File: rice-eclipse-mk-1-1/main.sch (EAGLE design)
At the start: 4 parts

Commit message: Added some new voltage regulators and used them. I also did something else, but I'm not sure what it was.
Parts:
- added ADC_X: AD7124-8BCPZ, analog-devices-extra-AD7124-8BCPZ:AD7124-8BCPZ
- added C3: 1UF, resistor:C-USC0603
- added C4, C6, C7: 10UF, rcl:C-US025-050X050
- added C5: 100UF, rcl:C-US025-050X050
- added REG1: AP2210N-3.3TRG1, diodes-extra:AP2210N-3.3TRG1
- added U1: LM1084ISX-5.0/NOPB, texas-extra:LM1084ISX-5.0/NOPB
- ADC1: value AD7124-8BCPZ -> MCP3208SN; device analog-devices-extra-AD7124-8BCPZ:AD7124-8BCPZ -> microchip-extra:MCP3208SN
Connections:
- new net +5V: C7.1, U1.VOUT
- new net AGND: ADC1.AGND, C3.2
- net +12V: now also C5.1, C6.1, REG1.VIN, U1.VIN
- net +3.3V: now also ADC1.VDD, ADC1.VREF, ADC_X.AVDD, ADC_X.IOVDD, C3.1, C4.1, REG1.VOUT; no longer ADC1.AVDD, ADC1.IOVDD
- net ADC1_A0: now also ADC1.CH0, ADC_X.AIN0/IOUT/VBIAS; no longer ADC1.AIN0/IOUT/VBIAS
- net ADC1_A1: now also ADC1.CH1, ADC_X.AIN1/IOUT/VBIAS; no longer ADC1.AIN1/IOUT/VBIAS
- net ADC1_A10: now also ADC_X.AIN10/IOUT/VBIAS; no longer ADC1.AIN10/IOUT/VBIAS
- net ADC1_A11: now also ADC_X.AIN11/IOUT/VBIAS; no longer ADC1.AIN11/IOUT/VBIAS
- net ADC1_A12: now also ADC_X.AIN12/IOUT/VBIAS; no longer ADC1.AIN12/IOUT/VBIAS
- net ADC1_A14: now also ADC_X.AIN14/IOUT/VBIAS/REFIN2(+); no longer ADC1.AIN14/IOUT/VBIAS/REFIN2(+)
- net ADC1_A15: now also ADC_X.AIN15/IOUT/VBIAS/REFIN2(-); no longer ADC1.AIN15/IOUT/VBIAS/REFIN2(-)
- net ADC1_A2: now also ADC1.CH2, ADC_X.AIN2/IOUT/VBIAS/P1; no longer ADC1.AIN2/IOUT/VBIAS/P1
- net ADC1_A3: now also ADC1.CH3, ADC_X.AIN3/IOUT/VBIAS/P2; no longer ADC1.AIN3/IOUT/VBIAS/P2
- net ADC1_A4: now also ADC1.CH4, ADC_X.AIN4/IOUT/VBIAS/P3; no longer ADC1.AIN4/IOUT/VBIAS/P3
- net ADC1_A5: now also ADC1.CH5, ADC_X.AIN5/IOUT/VBIAS/P4; no longer ADC1.AIN5/IOUT/VBIAS/P4
- net ADC1_A6: now also ADC1.CH6, ADC_X.AIN6/IOUT/VBIAS; no longer ADC1.AIN6/IOUT/VBIAS
- net ADC1_A7: now also ADC1.CH7, ADC_X.AIN7/IOUT/VBIAS; no longer ADC1.AIN7/IOUT/VBIAS
- net ADC1_A8: now also ADC_X.AIN8/IOUT/VBIAS; no longer ADC1.AIN8/IOUT/VBIAS
- net ADC1_A9: now also ADC_X.AIN9/IOUT/VBIAS; no longer ADC1.AIN9/IOUT/VBIAS
- net CS: now also ADC_X.*CS; no longer ADC1.*CS
- net DGND: now also ADC_X.AVSS, ADC_X.DGND, ADC_X.EP; no longer ADC1.AVSS, ADC1.EP
- net GND: now also C4.2, C5.2, C6.2, C7.2, REG1.GND, U1.GND
- net MISO: now also ADC_X.DOUT/*RDY; no longer ADC1.DOUT/*RDY
- net MOSI: now also ADC_X.DIN; no longer ADC1.DIN
- net N$1: now also ADC_X.REGCAPD; no longer ADC1.REGCAPD
- net N$2: now also ADC_X.REGCAPA; no longer ADC1.REGCAPA
- net SCLK: now also ADC_X.SCLK; no longer ADC1.SCLK

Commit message: Added a shorts library and some skeleton sheets in the schematic. Should provide a good environment for working on project.
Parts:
- removed ADC_X: AD7124-8BCPZ, analog-devices-extra-AD7124-8BCPZ:AD7124-8BCPZ
- removed C1, C2: 0.1UF, resistor:C-USC0603
- added SH1: SHORTT5, shorts:SHORTT5
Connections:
- removed net +3.3V: ADC1.VDD, ADC1.VREF, ADC_X.AVDD, ADC_X.IOVDD, C3.1, C4.1, REG1.VOUT
- removed net ADC1_A10: ADC_X.AIN10/IOUT/VBIAS
- removed net ADC1_A11: ADC_X.AIN11/IOUT/VBIAS
- removed net ADC1_A12: ADC_X.AIN12/IOUT/VBIAS
- removed net ADC1_A14: ADC_X.AIN14/IOUT/VBIAS/REFIN2(+)
- removed net ADC1_A15: ADC_X.AIN15/IOUT/VBIAS/REFIN2(-)
- removed net ADC1_A8: ADC_X.AIN8/IOUT/VBIAS
- removed net ADC1_A9: ADC_X.AIN9/IOUT/VBIAS
- removed net CS: ADC_X.*CS
- removed net MISO: ADC_X.DOUT/*RDY
- removed net MOSI: ADC_X.DIN
- removed net N$1: ADC_X.REGCAPD, C2.1
- removed net N$2: ADC_X.REGCAPA, C1.1
- removed net SCLK: ADC_X.SCLK
- new net +3V3: ADC1.VDD, ADC1.VREF, C3.1, C4.1, REG1.VOUT
- new net TEST_NET_1: SH1.P$1
- new net TEST_NET_2: SH1.P$2
- net ADC1_A0: no longer ADC_X.AIN0/IOUT/VBIAS
- net ADC1_A1: no longer ADC_X.AIN1/IOUT/VBIAS
- net ADC1_A2: no longer ADC_X.AIN2/IOUT/VBIAS/P1
- net ADC1_A3: no longer ADC_X.AIN3/IOUT/VBIAS/P2
- net ADC1_A4: no longer ADC_X.AIN4/IOUT/VBIAS/P3
- net ADC1_A5: no longer ADC_X.AIN5/IOUT/VBIAS/P4
- net ADC1_A6: no longer ADC_X.AIN6/IOUT/VBIAS
- net ADC1_A7: no longer ADC_X.AIN7/IOUT/VBIAS
- net DGND: no longer ADC_X.AVSS, ADC_X.DGND, ADC_X.EP, C1.2, C2.2

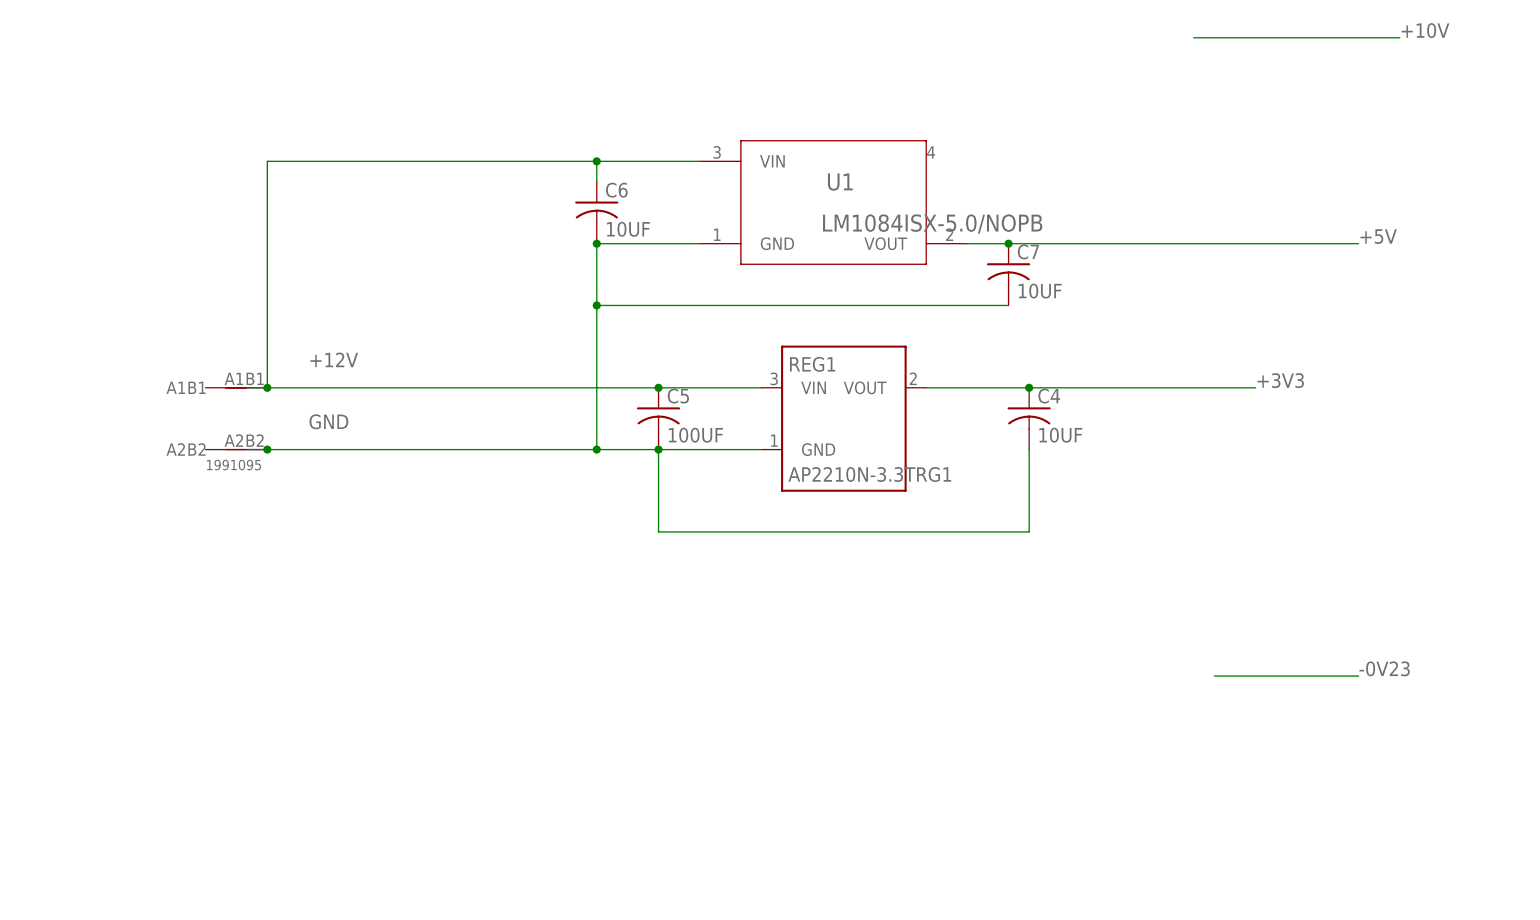
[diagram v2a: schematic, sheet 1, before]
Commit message: Added voltage regulator for -0.23v
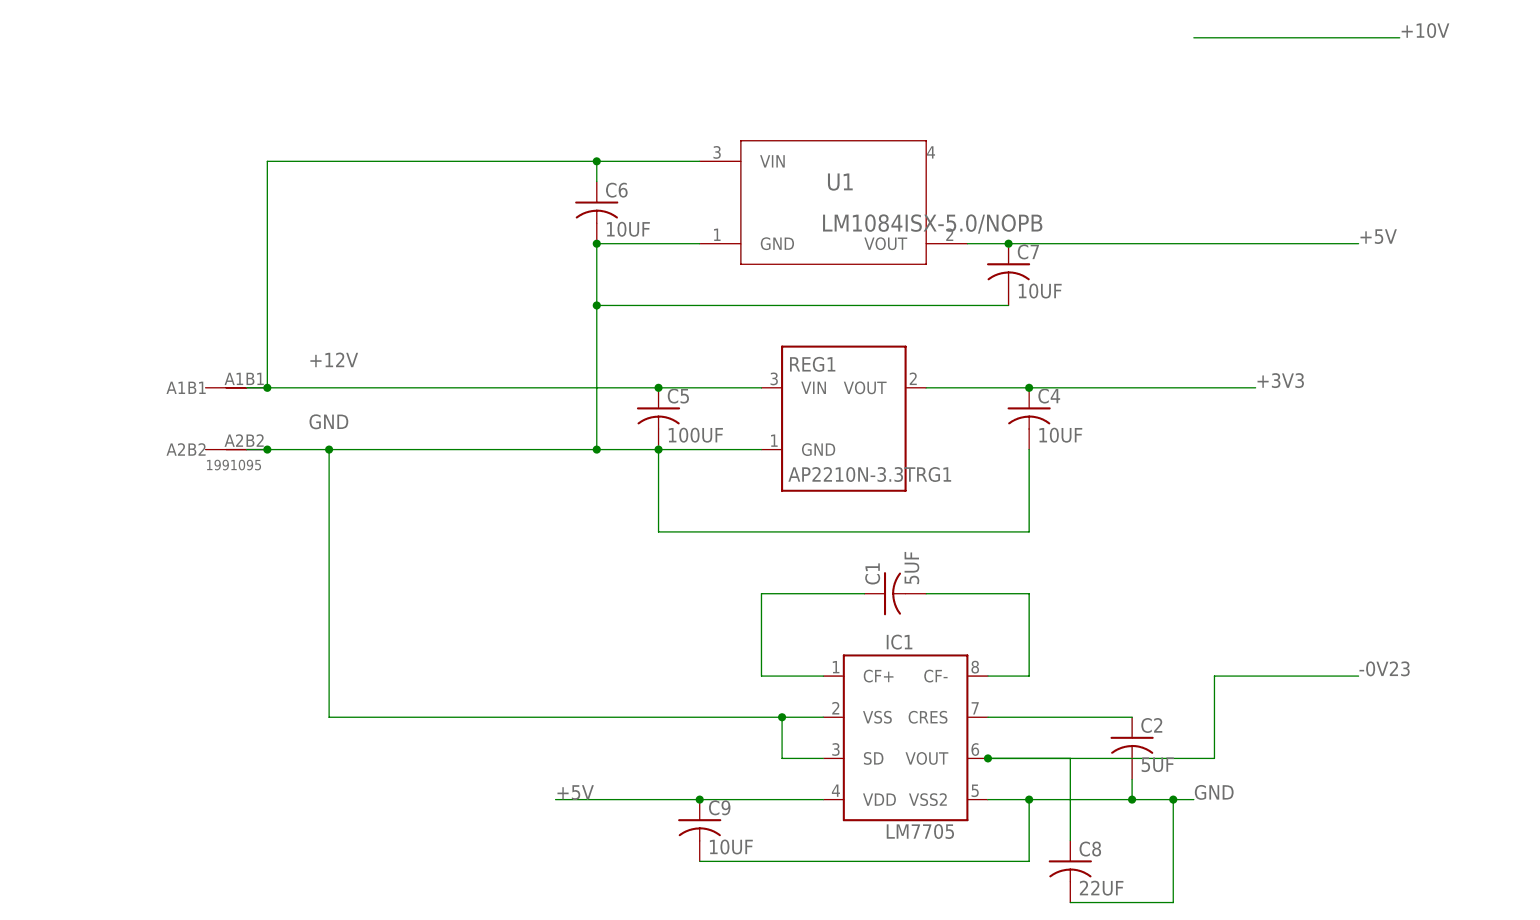
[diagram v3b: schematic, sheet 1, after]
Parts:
- added C1, C2: 5UF, rcl:C-USC0603
- added C8: 22UF, rcl:C-USC0603
- added C9: 10UF, rcl:C-USC0603
- added IC1: LM7705, texas-extra:LM7705
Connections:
- new net -0V23: C8.1, IC1.VOUT
- new net N$1: C1.1, IC1.CF+
- new net N$2: C1.2, IC1.CF-
- new net N$3: C2.1, IC1.CRES
- net +5V: now also C9.1, IC1.VDD
- net GND: now also C2.2, C8.2, C9.2, IC1.SD, IC1.VSS, IC1.VSS2
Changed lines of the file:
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@@
 <part name="FRAME7" library="frames" library_urn="urn:adsk.eagle:library:229" deviceset="A4L-LOC" device=""/>
 <part name="FRAME8" library="frames" library_urn="urn:adsk.eagle:library:229" deviceset="A4L-LOC" device=""/>
+<part name="IC1" library="texas-extra" deviceset="LM7705" device=""/>
+<part name="C1" library="rcl" library_urn="urn:adsk.eagle:library:334" deviceset="C-US" device="C0603" package3d_urn="urn:adsk.eagle:package:23616/2" value="5UF"/>
+<part name="C2" library="rcl" library_urn="urn:adsk.eagle:library:334" deviceset="C-US" device="C0603" package3d_urn="urn:adsk.eagle:package:23616/2" value="5UF"/>
+<part name="C8" library="rcl" library_urn="urn:adsk.eagle:library:334" deviceset="C-US" device="C0603" package3d_urn="urn:adsk.eagle:package:23616/2" value="22UF"/>
+<part name="C9" library="rcl" library_urn="urn:adsk.eagle:library:334" deviceset="C-US" device="C0603" package3d_urn="urn:adsk.eagle:package:23616/2" value="10UF"/>
 </parts>
 <sheets>
@@
 <attribute name="SHEET" x="230.505" y="5.08" size="2.54" layer="94"/>
 </instance>
+<instance part="IC1" gate="G$1" x="157.48" y="50.8"/>
+<instance part="C1" gate="G$1" x="154.94" y="68.58" rot="R90"/>
+<instance part="C2" gate="G$1" x="185.42" y="50.8"/>
+<instance part="C8" gate="G$1" x="177.8" y="35.56"/>
+<instance part="C9" gate="G$1" x="132.08" y="40.64"/>
 </instances>
 <busses>
@@
 <pinref part="C5" gate="G$1" pin="2"/>
 <junction x="127" y="86.36"/>
-<wire x1="119.38" y1="86.36" x2="78.74" y2="86.36" width="0.1524" layer="91"/>
+<wire x1="119.38" y1="86.36" x2="86.36" y2="86.36" width="0.1524" layer="91"/>
+<wire x1="86.36" y1="86.36" x2="78.74" y2="86.36" width="0.1524" layer="91"/>
 <wire x1="127" y1="86.36" x2="127" y2="76.2" width="0.1524" layer="91"/>
 <pinref part="C4" gate="G$1" pin="2"/>
@@
 <wire x1="170.18" y1="104.14" x2="119.38" y2="104.14" width="0.1524" layer="91"/>
 <junction x="119.38" y="104.14"/>
+<pinref part="IC1" gate="G$1" pin="VSS"/>
+<wire x1="147.32" y1="53.34" x2="142.24" y2="53.34" width="0.1524" layer="91"/>
+<wire x1="142.24" y1="53.34" x2="86.36" y2="53.34" width="0.1524" layer="91"/>
+<wire x1="86.36" y1="53.34" x2="86.36" y2="86.36" width="0.1524" layer="91"/>
+<junction x="86.36" y="86.36"/>
+<pinref part="IC1" gate="G$1" pin="SD"/>
+<wire x1="147.32" y1="48.26" x2="142.24" y2="48.26" width="0.1524" layer="91"/>
+<wire x1="142.24" y1="48.26" x2="142.24" y2="53.34" width="0.1524" layer="91"/>
+<junction x="142.24" y="53.34"/>
+</segment>
+<segment>
+<pinref part="IC1" gate="G$1" pin="VSS2"/>
+<wire x1="167.64" y1="43.18" x2="172.72" y2="43.18" width="0.1524" layer="91"/>
+<label x="193.04" y="43.18" size="1.778" layer="95"/>
+<pinref part="C9" gate="G$1" pin="2"/>
+<wire x1="172.72" y1="43.18" x2="185.42" y2="43.18" width="0.1524" layer="91"/>
+<wire x1="185.42" y1="43.18" x2="190.5" y2="43.18" width="0.1524" layer="91"/>
+<wire x1="190.5" y1="43.18" x2="193.04" y2="43.18" width="0.1524" layer="91"/>
+<wire x1="132.08" y1="35.56" x2="172.72" y2="35.56" width="0.1524" layer="91"/>
+<wire x1="172.72" y1="35.56" x2="172.72" y2="43.18" width="0.1524" layer="91"/>
+<junction x="172.72" y="43.18"/>
+<pinref part="C2" gate="G$1" pin="2"/>
+<wire x1="185.42" y1="45.72" x2="185.42" y2="43.18" width="0.1524" layer="91"/>
+<junction x="185.42" y="43.18"/>
+<pinref part="C8" gate="G$1" pin="2"/>
+<wire x1="177.8" y1="30.48" x2="190.5" y2="30.48" width="0.1524" layer="91"/>
+<wire x1="190.5" y1="30.48" x2="190.5" y2="43.18" width="0.1524" layer="91"/>
+<junction x="190.5" y="43.18"/>
 </segment>
 </net>
@@
 <junction x="170.18" y="111.76"/>
 </segment>
+<segment>
+<pinref part="IC1" gate="G$1" pin="VDD"/>
+<pinref part="C9" gate="G$1" pin="1"/>
+<wire x1="147.32" y1="43.18" x2="132.08" y2="43.18" width="0.1524" layer="91"/>
+<wire x1="132.08" y1="43.18" x2="114.3" y2="43.18" width="0.1524" layer="91"/>
+<junction x="132.08" y="43.18"/>
+<label x="114.3" y="43.18" size="1.778" layer="95"/>
+</segment>
 </net>
 <net name="-0V23" class="0">
@@
 <wire x1="195.58" y1="58.42" x2="213.36" y2="58.42" width="0.1524" layer="91"/>
 <label x="213.36" y="58.42" size="1.778" layer="95"/>
+<pinref part="IC1" gate="G$1" pin="VOUT"/>
+<pinref part="C8" gate="G$1" pin="1"/>
+<wire x1="167.64" y1="48.26" x2="177.8" y2="48.26" width="0.1524" layer="91"/>
+<wire x1="177.8" y1="48.26" x2="177.8" y2="38.1" width="0.1524" layer="91"/>
+<wire x1="167.64" y1="48.26" x2="195.58" y2="48.26" width="0.1524" layer="91"/>
+<wire x1="195.58" y1="48.26" x2="195.58" y2="58.42" width="0.1524" layer="91"/>
+<junction x="167.64" y="48.26"/>
 </segment>
 </net>
@@
 </segment>
 </net>
+<net name="N$1" class="0">
+<segment>
+<pinref part="C1" gate="G$1" pin="1"/>
+<wire x1="152.4" y1="68.58" x2="139.7" y2="68.58" width="0.1524" layer="91"/>
+<wire x1="139.7" y1="68.58" x2="139.7" y2="58.42" width="0.1524" layer="91"/>
+<pinref part="IC1" gate="G$1" pin="CF+"/>
+<wire x1="139.7" y1="58.42" x2="147.32" y2="58.42" width="0.1524" layer="91"/>
+</segment>
+</net>
+<net name="N$2" class="0">
+<segment>
+<pinref part="C1" gate="G$1" pin="2"/>
+<wire x1="160.02" y1="68.58" x2="172.72" y2="68.58" width="0.1524" layer="91"/>
+<wire x1="172.72" y1="68.58" x2="172.72" y2="58.42" width="0.1524" layer="91"/>
+<pinref part="IC1" gate="G$1" pin="CF-"/>
+<wire x1="172.72" y1="58.42" x2="167.64" y2="58.42" width="0.1524" layer="91"/>
+</segment>
+</net>
+<net name="N$3" class="0">
+<segment>
+<pinref part="IC1" gate="G$1" pin="CRES"/>
+<pinref part="C2" gate="G$1" pin="1"/>
+<wire x1="167.64" y1="53.34" x2="185.42" y2="53.34" width="0.1524" layer="91"/>
+</segment>
+</net>

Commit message: edited wire
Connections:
- new net N$4: U1.4
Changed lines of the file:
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@@
 <?xml version="1.0" encoding="utf-8"?>
 <!DOCTYPE eagle SYSTEM "eagle.dtd">
-<eagle version="8.3.1">
+<eagle version="8.2.2">
 <drawing>
 <settings>
@@
 <part name="FRAME3" library="frames" library_urn="urn:adsk.eagle:library:229" deviceset="A4L-LOC" device=""/>
 <part name="ADC1" library="microchip-extra" deviceset="MCP3208" device="SN"/>
-<part name="C3" library="resistor" library_urn="urn:adsk.eagle:library:348" deviceset="C-US" device="C0603" package3d_urn="urn:adsk.eagle:package:26138/1" value="1UF"/>
+<part name="C3" library="resistor" library_urn="urn:adsk.eagle:library:348" deviceset="C-US" device="C0603" value="1UF"/>
 <part name="REG1" library="diodes-extra" deviceset="AP2210N-3.3TRG1" device=""/>
-<part name="C4" library="rcl" library_urn="urn:adsk.eagle:library:334" deviceset="C-US" device="025-050X050" package3d_urn="urn:adsk.eagle:package:23633/1" value="10UF"/>
-<part name="C5" library="rcl" library_urn="urn:adsk.eagle:library:334" deviceset="C-US" device="025-050X050" package3d_urn="urn:adsk.eagle:package:23633/1" value="100UF"/>
+<part name="C4" library="rcl" library_urn="urn:adsk.eagle:library:334" deviceset="C-US" device="025-050X050" value="10UF"/>
+<part name="C5" library="rcl" library_urn="urn:adsk.eagle:library:334" deviceset="C-US" device="025-050X050" value="100UF"/>
 <part name="U1" library="texas-extra" deviceset="LM1084ISX-5.0/NOPB" device=""/>
-<part name="C6" library="rcl" library_urn="urn:adsk.eagle:library:334" deviceset="C-US" device="025-050X050" package3d_urn="urn:adsk.eagle:package:23633/1" value="10UF"/>
-<part name="C7" library="rcl" library_urn="urn:adsk.eagle:library:334" deviceset="C-US" device="025-050X050" package3d_urn="urn:adsk.eagle:package:23633/1" value="10UF"/>
+<part name="C6" library="rcl" library_urn="urn:adsk.eagle:library:334" deviceset="C-US" device="025-050X050" value="10UF"/>
+<part name="C7" library="rcl" library_urn="urn:adsk.eagle:library:334" deviceset="C-US" device="025-050X050" value="10UF"/>
 <part name="FRAME4" library="frames" library_urn="urn:adsk.eagle:library:229" deviceset="A4L-LOC" device=""/>
 <part name="FRAME5" library="frames" library_urn="urn:adsk.eagle:library:229" deviceset="A4L-LOC" device=""/>
@@
 <part name="FRAME8" library="frames" library_urn="urn:adsk.eagle:library:229" deviceset="A4L-LOC" device=""/>
 <part name="IC1" library="texas-extra" deviceset="LM7705" device=""/>
-<part name="C1" library="rcl" library_urn="urn:adsk.eagle:library:334" deviceset="C-US" device="C0603" package3d_urn="urn:adsk.eagle:package:23616/2" value="5UF"/>
-<part name="C2" library="rcl" library_urn="urn:adsk.eagle:library:334" deviceset="C-US" device="C0603" package3d_urn="urn:adsk.eagle:package:23616/2" value="5UF"/>
-<part name="C8" library="rcl" library_urn="urn:adsk.eagle:library:334" deviceset="C-US" device="C0603" package3d_urn="urn:adsk.eagle:package:23616/2" value="22UF"/>
-<part name="C9" library="rcl" library_urn="urn:adsk.eagle:library:334" deviceset="C-US" device="C0603" package3d_urn="urn:adsk.eagle:package:23616/2" value="10UF"/>
+<part name="C1" library="rcl" library_urn="urn:adsk.eagle:library:334" deviceset="C-US" device="C0603" value="5UF"/>
+<part name="C2" library="rcl" library_urn="urn:adsk.eagle:library:334" deviceset="C-US" device="C0603" value="5UF"/>
+<part name="C8" library="rcl" library_urn="urn:adsk.eagle:library:334" deviceset="C-US" device="C0603" value="22UF"/>
+<part name="C9" library="rcl" library_urn="urn:adsk.eagle:library:334" deviceset="C-US" device="C0603" value="10UF"/>
 </parts>
 <sheets>
@@
 </segment>
 </net>
+<net name="N$4" class="0">
+<segment>
+<pinref part="U1" gate="A" pin="4"/>
+<wire x1="160.02" y1="121.92" x2="170.18" y2="121.92" width="0.1524" layer="91"/>
+</segment>
+</net>
 </nets>
 </sheet>
@@
 <compatibility>
 <note version="8.2" severity="warning">
-Since Version 8.2, EAGLE supports online libraries. The ids
+Since Version 8.2, Eagle supports online libraries. The ids
 of those online libraries will not be understood (or retained)
 with this version.
 </note>
-<note version="8.3" severity="warning">
-Since Version 8.3, EAGLE supports URNs for individual library
-assets (packages, symbols, and devices). The URNs of those assets
-will not be understood (or retained) with this version.
-</note>
-<note version="8.3" severity="warning">
-Since Version 8.3, EAGLE supports the association of 3D packages
-with devices in libraries, schematics, and board files. Those 3D
-packages will not be understood (or retained) with this version.
-</note>
 </compatibility>

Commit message: Added a new sheet for external connectors.
Added raspberry PI GPIO to the sheet.
Will probably add any outputs and inputs soon.
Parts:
- added X1: 2540-5, con-3m:2540-5
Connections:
- new net RPI_GPIO_1: X1-1.KL
- new net RPI_GPIO_10: X1-10.KL
- new net RPI_GPIO_11: X1-11.KL
- new net RPI_GPIO_12: X1-12.KL
- new net RPI_GPIO_13: X1-13.KL
- new net RPI_GPIO_14: X1-14.KL
- new net RPI_GPIO_15: X1-15.KL
- new net RPI_GPIO_16: X1-16.KL
- new net RPI_GPIO_17: X1-17.KL
- new net RPI_GPIO_18: X1-18.KL
- new net RPI_GPIO_19: X1-19.KL
- new net RPI_GPIO_2: X1-2.KL
- new net RPI_GPIO_20: X1-20.KL
- new net RPI_GPIO_21: X1-21.KL
- new net RPI_GPIO_22: X1-22.KL
- new net RPI_GPIO_23: X1-23.KL
- new net RPI_GPIO_24: X1-24.KL
- new net RPI_GPIO_25: X1-25.KL
- new net RPI_GPIO_26: X1-26.KL
- new net RPI_GPIO_27: X1-27.KL
- new net RPI_GPIO_28: X1-28.KL
- new net RPI_GPIO_29: X1-29.KL
- new net RPI_GPIO_3: X1-3.KL
- new net RPI_GPIO_30: X1-30.KL
- new net RPI_GPIO_31: X1-31.KL
- new net RPI_GPIO_32: X1-32.KL
- new net RPI_GPIO_33: X1-33.KL
- new net RPI_GPIO_34: X1-34.KL
- new net RPI_GPIO_35: X1-35.KL
- new net RPI_GPIO_36: X1-36.KL
- new net RPI_GPIO_37: X1-37.KL
- new net RPI_GPIO_38: X1-38.KL
- new net RPI_GPIO_39: X1-39.KL
- new net RPI_GPIO_4: X1-4.KL
- new net RPI_GPIO_40: X1-40.KL
- new net RPI_GPIO_5: X1-5.KL
- new net RPI_GPIO_6: X1-6.KL
- new net RPI_GPIO_7: X1-7.KL
- new net RPI_GPIO_8: X1-8.KL
- new net RPI_GPIO_9: X1-9.KL
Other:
- note added: "RPI GPIO"
